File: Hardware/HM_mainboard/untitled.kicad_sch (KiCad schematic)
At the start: 13 parts, among them J1 JST PH2P ST90, Q1 PMOS AS3401, U1 MCP73831-2, U2 TC1262-33

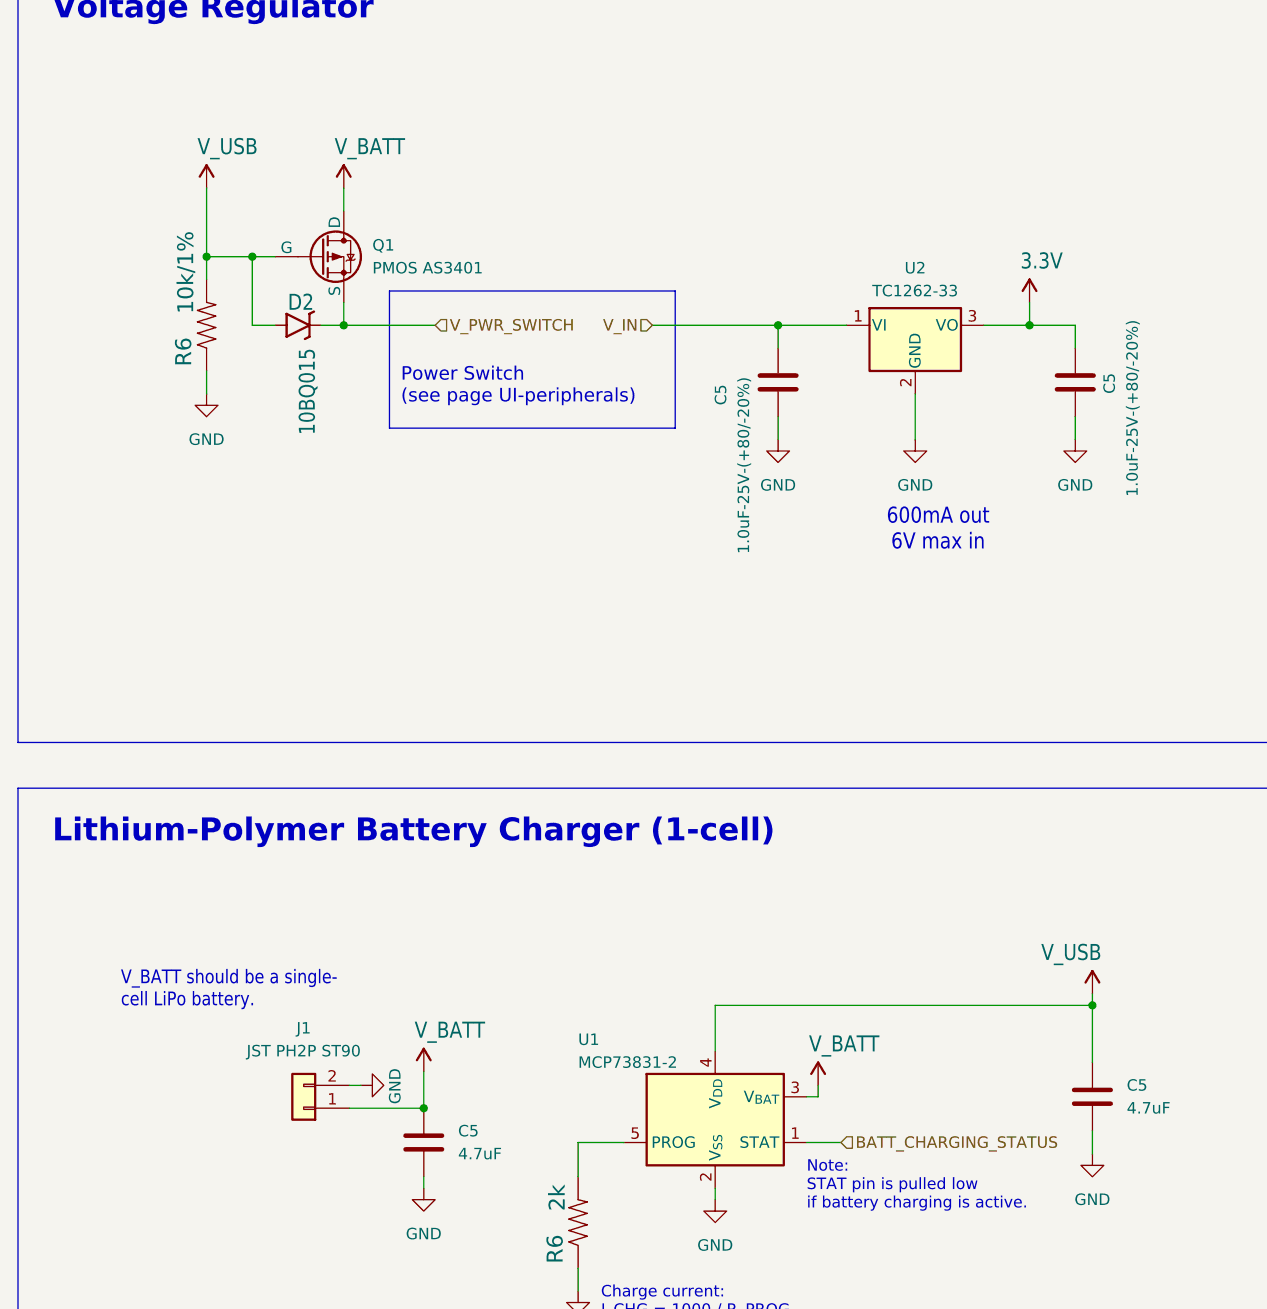
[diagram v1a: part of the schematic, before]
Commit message: Added testpoints to pcb
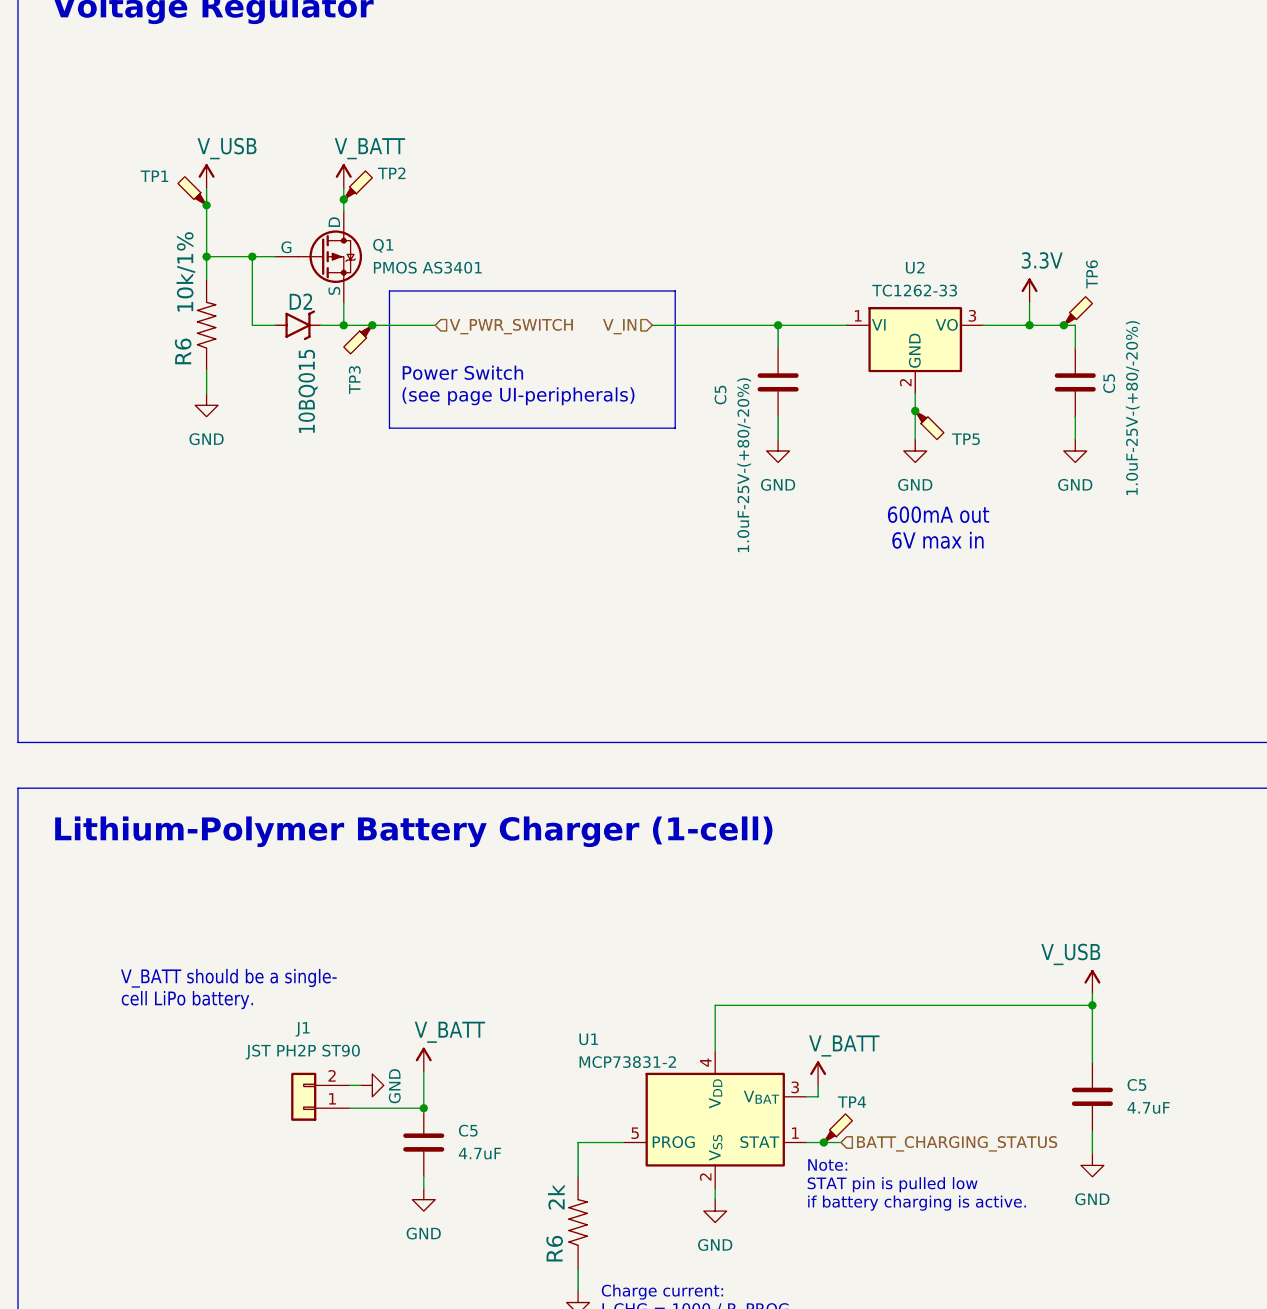
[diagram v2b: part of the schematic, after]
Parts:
- added TP1, TP2, TP3, TP4, TP5, TP6: TestPoint_Probe, TestPoint:TestPoint_THTPad_D2.0mm_Drill1.0mm, symbol Connector:TestPoint_Probe
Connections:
- net 3.3V: now also TP6.1
- net BATT_CHARGING_STATUS: now also TP4.1
- net GND: now also TP5.1
- net V_BATT: now also TP2.1
- net V_PWR_SWITCH: now also TP3.1
- net V_USB: now also TP1.1
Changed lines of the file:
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@@
   (junction (at 132.715 59.055) (diameter 0) (color 0 0 0 0)
   )
+  (junction (at 120.015 68.58) (diameter 0) (color 0 0 0 0)
+  )
+  (junction (at 56.515 45.085) (diameter 0) (color 0 0 0 0)
+  )
+  (junction (at 109.855 149.86) (diameter 0) (color 0 0 0 0)
+  )
+  (junction (at 41.275 45.72) (diameter 0) (color 0 0 0 0)
+  )
   (junction (at 56.515 59.055) (diameter 0) (color 0 0 0 0)
   )
@@
   (junction (at 46.355 51.435) (diameter 0) (color 0 0 0 0)
   )
+  (junction (at 136.525 59.055) (diameter 0) (color 0 0 0 0)
+  )
+  (junction (at 59.69 59.055) (diameter 0) (color 0 0 0 0)
+  )
   (wire (pts (xy 97.79 156.21) (xy 97.79 154.94))
     (stroke (width 0) (type default))
@@
     (stroke (width 0.1524) (type solid))
   )
-  (wire (pts (xy 41.275 43.815) (xy 41.275 51.435))
+  (wire (pts (xy 41.275 43.815) (xy 41.275 45.72))
+    (stroke (width 0.1524) (type solid))
+  )
+  (wire (pts (xy 41.275 45.72) (xy 41.275 51.435))
     (stroke (width 0.1524) (type solid))
   )
@@
     (stroke (width 0) (type default))
   )
+  (wire (pts (xy 56.515 45.085) (xy 56.515 46.355))
+    (stroke (width 0.1524) (type solid))
+  )
+  (wire (pts (xy 120.015 68.58) (xy 120.015 71.755))
+    (stroke (width 0) (type default))
+  )
   (wire (pts (xy 65.405 141.986) (xy 65.405 146.05))
     (stroke (width 0.1524) (type solid))
@@
     (stroke (width 0) (type default))
   )
+  (wire (pts (xy 136.525 59.055) (xy 137.795 59.055))
+    (stroke (width 0.1524) (type solid))
+  )
   (wire (pts (xy 46.355 51.435) (xy 41.275 51.435))
     (stroke (width 0.1524) (type solid))
@@
     (stroke (width 0.1524) (type solid))
   )
+  (wire (pts (xy 59.69 59.055) (xy 66.675 59.055))
+    (stroke (width 0) (type default))
+  )
   (wire (pts (xy 41.275 66.675) (xy 41.275 64.135))
     (stroke (width 0.1524) (type solid))
@@
     (stroke (width 0) (type default))
   )
-  (wire (pts (xy 120.015 66.675) (xy 120.015 71.755))
+  (wire (pts (xy 120.015 66.675) (xy 120.015 68.58))
     (stroke (width 0) (type default))
   )
@@
     (stroke (width 0.1524) (type solid))
   )
-  (wire (pts (xy 111.76 149.86) (xy 107.95 149.86))
-    (stroke (width 0) (type default))
-  )
-  (wire (pts (xy 132.715 59.055) (xy 137.795 59.055))
+  (wire (pts (xy 111.76 149.86) (xy 109.855 149.86))
+    (stroke (width 0) (type default))
+  )
+  (wire (pts (xy 132.715 59.055) (xy 136.525 59.055))
     (stroke (width 0.1524) (type solid))
   )
@@
     (stroke (width 0.1524) (type solid))
   )
-  (wire (pts (xy 56.515 59.055) (xy 66.675 59.055))
+  (wire (pts (xy 56.515 59.055) (xy 59.69 59.055))
     (stroke (width 0) (type default))
   )
@@
     (stroke (width 0.1524) (type solid))
   )
-  (wire (pts (xy 56.515 43.815) (xy 56.515 46.355))
+  (wire (pts (xy 56.515 43.815) (xy 56.515 45.085))
     (stroke (width 0.1524) (type solid))
   )
@@
   )
   (wire (pts (xy 107.95 144.78) (xy 109.22 144.78))
+    (stroke (width 0) (type default))
+  )
+  (wire (pts (xy 109.855 149.86) (xy 107.95 149.86))
     (stroke (width 0) (type default))
   )
@@
     )
   )
+  (symbol (lib_id "Connector:TestPoint_Probe") (at 120.015 68.58 270) (unit 1)
+    (in_bom yes) (on_board yes) (dnp no)
+    (property "Reference" "TP5" (at 125.73 71.755 90)
+      (effects (font (size 1.27 1.27)))
+    )
+    (property "Value" "TestPoint_Probe" (at 131.445 69.85 90)
+      (effects (font (size 1.27 1.27)) hide)
+    )
+    (property "Footprint" "TestPoint:TestPoint_THTPad_D2.0mm_Drill1.0mm" (at 120.015 73.66 0)
+      (effects (font (size 1.27 1.27)) hide)
+    )
+    (property "Datasheet" "~" (at 120.015 73.66 0)
+      (effects (font (size 1.27 1.27)) hide)
+    )
+    (pin "1")
+    (instances
+      (project "HM_mainboard"
+        (path "/54a6df43-5475-46a2-9916-8b0260700d4c/b19d5209-4861-4a96-a3d1-daca4a23de52"
+          (reference "TP5") (unit 1)
+        )
+      )
+    )
+  )
   (symbol (lib_id "Device:C") (at 137.795 65.405 0) (unit 1)
     (in_bom yes) (on_board yes) (dnp no)
@@
         (path "/54a6df43-5475-46a2-9916-8b0260700d4c/b19d5209-4861-4a96-a3d1-daca4a23de52"
           (reference "C3") (unit 1)
+        )
+      )
+    )
+  )
+  (symbol (lib_id "Connector:TestPoint_Probe") (at 59.69 59.055 180) (unit 1)
+    (in_bom yes) (on_board yes) (dnp no)
+    (property "Reference" "TP3" (at 57.785 66.675 90)
+      (effects (font (size 1.27 1.27)) (justify right))
+    )
+    (property "Value" "TestPoint_Probe" (at 59.69 78.105 90)
+      (effects (font (size 1.27 1.27)) (justify right) hide)
+    )
+    (property "Footprint" "TestPoint:TestPoint_THTPad_D2.0mm_Drill1.0mm" (at 54.61 59.055 0)
+      (effects (font (size 1.27 1.27)) hide)
+    )
+    (property "Datasheet" "~" (at 54.61 59.055 0)
+      (effects (font (size 1.27 1.27)) hide)
+    )
+    (pin "1")
+    (instances
+      (project "HM_mainboard"
+        (path "/54a6df43-5475-46a2-9916-8b0260700d4c/b19d5209-4861-4a96-a3d1-daca4a23de52"
+          (reference "TP3") (unit 1)
         )
       )
@@
     )
   )
+  (symbol (lib_id "Connector:TestPoint_Probe") (at 136.525 59.055 0) (unit 1)
+    (in_bom yes) (on_board yes) (dnp no)
+    (property "Reference" "TP6" (at 139.7 53.34 90)
+      (effects (font (size 1.27 1.27)))
+    )
+    (property "Value" "TestPoint_Probe" (at 137.795 47.625 90)
+      (effects (font (size 1.27 1.27)) hide)
+    )
+    (property "Footprint" "TestPoint:TestPoint_THTPad_D2.0mm_Drill1.0mm" (at 141.605 59.055 0)
+      (effects (font (size 1.27 1.27)) hide)
+    )
+    (property "Datasheet" "~" (at 141.605 59.055 0)
+      (effects (font (size 1.27 1.27)) hide)
+    )
+    (pin "1")
+    (instances
+      (project "HM_mainboard"
+        (path "/54a6df43-5475-46a2-9916-8b0260700d4c/b19d5209-4861-4a96-a3d1-daca4a23de52"
+          (reference "TP6") (unit 1)
+        )
+      )
+    )
+  )
+  (symbol (lib_id "Connector:TestPoint_Probe") (at 56.515 45.085 0) (unit 1)
+    (in_bom yes) (on_board yes) (dnp no) (fields_autoplaced)
+    (property "Reference" "TP2" (at 60.325 42.2275 0)
+      (effects (font (size 1.27 1.27)) (justify left))
+    )
+    (property "Value" "TestPoint_Probe" (at 60.325 44.7675 0)
+      (effects (font (size 1.27 1.27)) (justify left) hide)
+    )
+    (property "Footprint" "TestPoint:TestPoint_THTPad_D2.0mm_Drill1.0mm" (at 61.595 45.085 0)
+      (effects (font (size 1.27 1.27)) hide)
+    )
+    (property "Datasheet" "~" (at 61.595 45.085 0)
+      (effects (font (size 1.27 1.27)) hide)
+    )
+    (pin "1")
+    (instances
+      (project "HM_mainboard"
+        (path "/54a6df43-5475-46a2-9916-8b0260700d4c/b19d5209-4861-4a96-a3d1-daca4a23de52"
+          (reference "TP2") (unit 1)
+        )
+      )
+    )
+  )
   (symbol (lib_id "esp32-thing-eagle-import:V_BATT") (at 200.66 123.19 0) (unit 1)
     (in_bom yes) (on_board yes) (dnp no)
@@
     )
   )
+  (symbol (lib_id "Connector:TestPoint_Probe") (at 41.275 45.72 90) (unit 1)
+    (in_bom yes) (on_board yes) (dnp no)
+    (property "Reference" "TP1" (at 35.56 42.545 90)
+      (effects (font (size 1.27 1.27)))
+    )
+    (property "Value" "TestPoint_Probe" (at 29.845 44.45 90)
+      (effects (font (size 1.27 1.27)) hide)
+    )
+    (property "Footprint" "TestPoint:TestPoint_THTPad_D2.0mm_Drill1.0mm" (at 41.275 40.64 0)
+      (effects (font (size 1.27 1.27)) hide)
+    )
+    (property "Datasheet" "~" (at 41.275 40.64 0)
+      (effects (font (size 1.27 1.27)) hide)
+    )
+    (pin "1")
+    (instances
+      (project "HM_mainboard"
+        (path "/54a6df43-5475-46a2-9916-8b0260700d4c/b19d5209-4861-4a96-a3d1-daca4a23de52"
+          (reference "TP1") (unit 1)
+        )
+      )
+    )
+  )
   (symbol (lib_id "esp32-thing-eagle-import:V_BATT") (at 56.515 43.815 0) (unit 1)
     (in_bom yes) (on_board yes) (dnp no)
@@
         )
       )
+    )
+  )
+  (symbol (lib_id "Connector:TestPoint_Probe") (at 109.855 149.86 0) (unit 1)
+    (in_bom yes) (on_board yes) (dnp no)
+    (property "Reference" "TP4" (at 113.03 145.415 0)
+      (effects (font (size 1.27 1.27)))
+    )
+    (property "Value" "TestPoint_Probe" (at 111.125 138.43 90)
+      (effects (font (size 1.27 1.27)) hide)
+    )
+    (property "Footprint" "TestPoint:TestPoint_THTPad_D2.0mm_Drill1.0mm" (at 114.935 149.86 0)
+      (effects (font (size 1.27 1.27)) hide)
+    )
+    (property "Datasheet" "~" (at 114.935 149.86 0)
+      (effects (font (size 1.27 1.27)) hide)
+    )
+    (pin "1")
+    (instances
+      (project "HM_mainboard"
+        (path "/54a6df43-5475-46a2-9916-8b0260700d4c/b19d5209-4861-4a96-a3d1-daca4a23de52"
+          (reference "TP4") (unit 1)
+        )
+      )

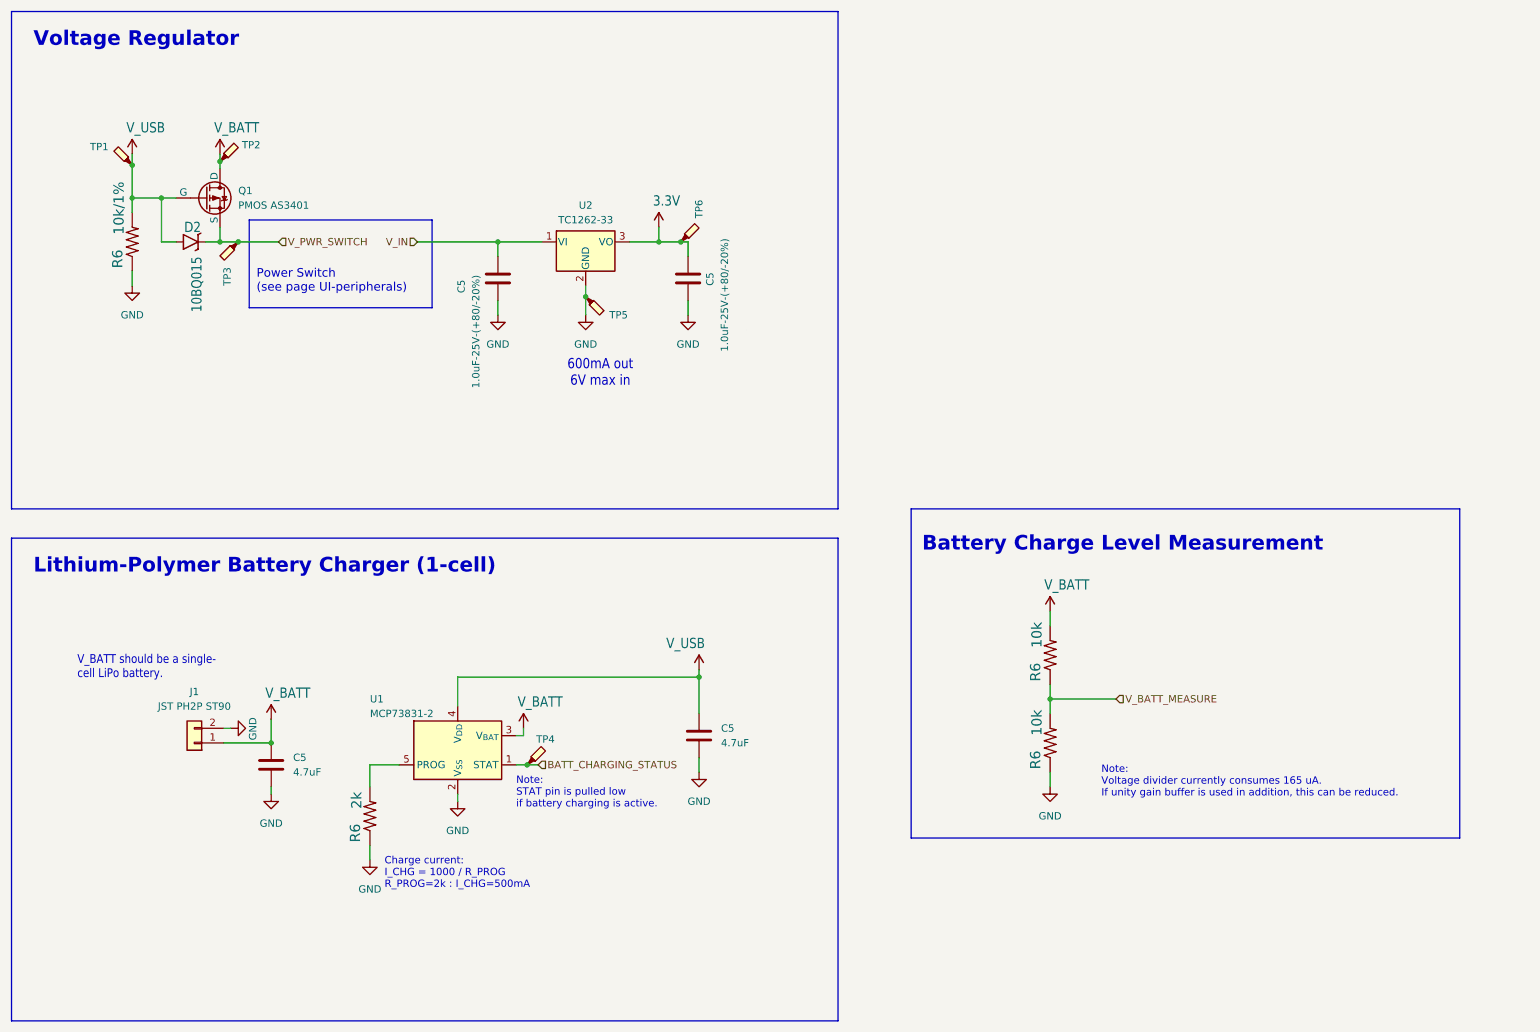
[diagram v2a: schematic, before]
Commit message: Updated schematic and PCB according to Email from BA on 16th of April
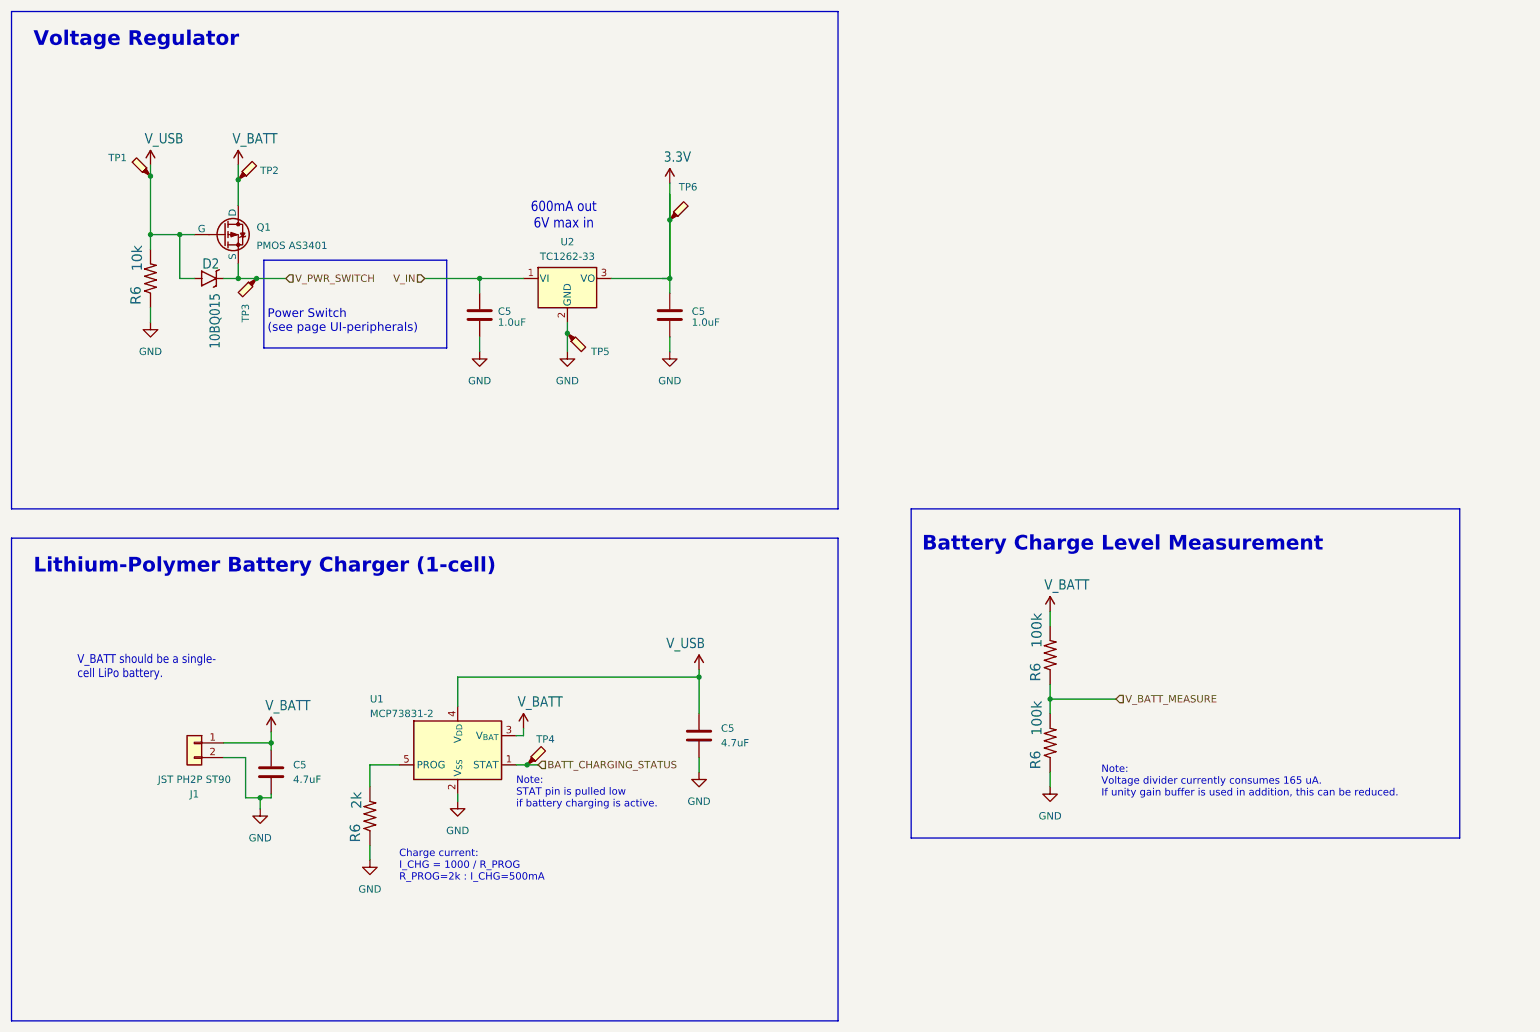
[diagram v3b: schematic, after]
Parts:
- C5: value 1.0uF-25V-(+80/-20%) -> 1.0uF
- R6: value 10k -> 100k
- R6: value 10k/1% -> 10k
- TP6: value TestPoint_Probe -> 3v3
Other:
- moved on the sheet: C5, D2, J1, Q1, R6, TP1, TP2, TP3, TP5, TP6, U2
